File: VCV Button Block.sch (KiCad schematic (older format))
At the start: 23 parts, among them J7 Conn_02x05_Odd_Even, SW41 B3F-5050, SW42 B3F-5050, SW43 B3F-5050, SW44 B3F-5050, SW45 B3F-5050, SW46 B3F-5050, SW47 B3F-5050, SW48 B3F-5050, SW49 B3F-5050, SW50 B3F-5050, SW51 B3F-5050, SW52 B3F-5050, SW53 B3F-5050, SW54 B3F-5050, SW55 B3F-5050, SW56 B3F-5050, U4 CD74HC4067M

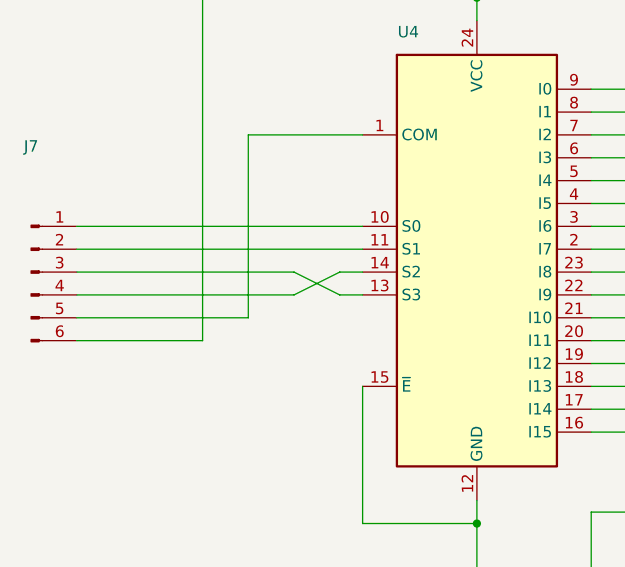
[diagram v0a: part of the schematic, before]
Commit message: Fixed S0-S3 Rail, added LEDS
Was an error on the schematic, easily fixed without changing the traces, glad I left it before deleting them all.

LEDs and relate resistors are in.
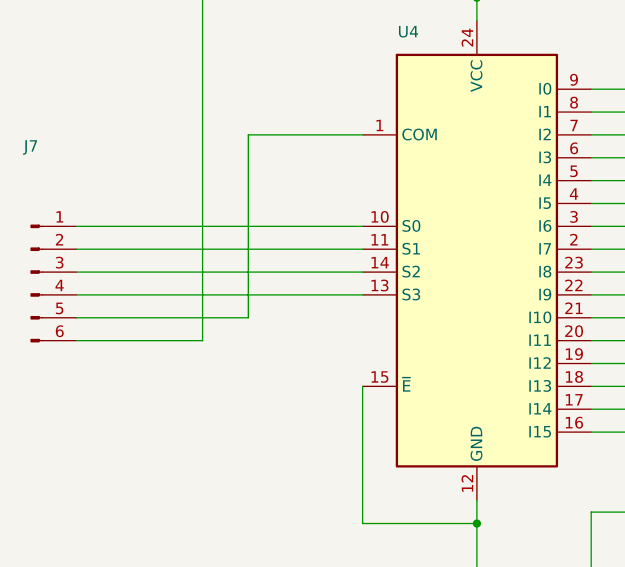
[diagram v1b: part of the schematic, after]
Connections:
- net at U4.13 (S3): now also J7.4 (Pin_4); no longer J7.3 (Pin_3)
- net at U4.14 (S2): now also J7.3 (Pin_3); no longer J7.4 (Pin_4)
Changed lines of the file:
@@
 	1500 1150 2700 1150
 Wire Wire Line
-	1900 2450 950  2450
+	950  2350 2200 2350
 Wire Wire Line
-	950  2350 1900 2350
-Wire Wire Line
-	2100 2350 2200 2350
-Wire Wire Line
-	2100 2450 2200 2450
-Wire Wire Line
-	1900 2350 2100 2450
-Wire Wire Line
-	2100 2350 1900 2450
+	950  2450 2200 2450
 $EndSCHEMATC

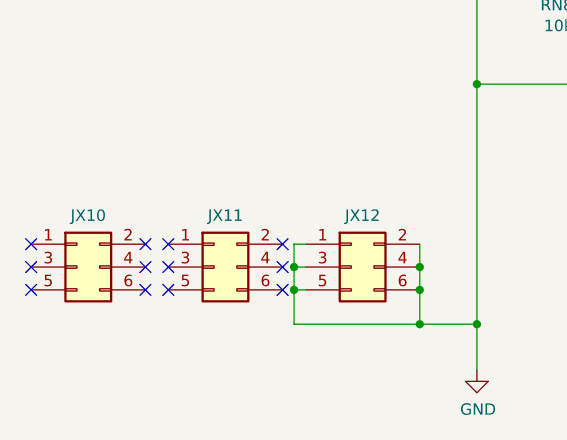
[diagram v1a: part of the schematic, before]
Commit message: Rails done, GND corrected.
Now for checking and decals
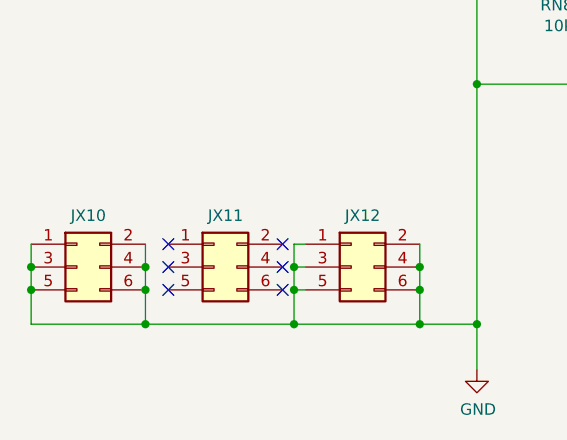
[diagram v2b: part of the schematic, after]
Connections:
- net GND: now also JX10.1 (Pin_1), JX10.2 (Pin_2), JX10.3 (Pin_3), JX10.4 (Pin_4), JX10.5 (Pin_5), JX10.6 (Pin_6)
- no-connect marks 44 -> 38
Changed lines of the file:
@@
 $Descr A4 11693 8268
 encoding utf-8
-Sheet 8 8
+Sheet 8 9
 Title ""
 Date ""
@@
 NoConn ~ 1350 6950
 NoConn ~ 1350 6850
-NoConn ~ 1250 6850
-NoConn ~ 1250 6950
-NoConn ~ 1250 7050
-NoConn ~ 750  6850
-NoConn ~ 750  6950
-NoConn ~ 750  7050
 Wire Wire Line
 	2700 3450 2700 6150
@@
 Wire Wire Line
 	950  2450 2200 2450
+Wire Wire Line
+	1250 6850 1250 6950
+Wire Wire Line
+	1250 7200 1900 7200
+Connection ~ 1250 6950
+Wire Wire Line
+	1250 6950 1250 7050
+Connection ~ 1250 7050
+Wire Wire Line
+	1250 7050 1250 7200
+Connection ~ 1900 7200
+Wire Wire Line
+	750  6850 750  6950
+Wire Wire Line
+	750  7200 1250 7200
+Connection ~ 750  6950
+Wire Wire Line
+	750  6950 750  7050
+Connection ~ 750  7050
+Wire Wire Line
+	750  7050 750  7200
+Connection ~ 1250 7200
 $EndSCHEMATC
